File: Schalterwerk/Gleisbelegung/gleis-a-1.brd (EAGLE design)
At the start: 100 x 80 mm, 34 parts, among them J1 PHNX_4P_508CONN_1017493, J2 PHNX_4P_508CONN_1017493, J3 PHNX_2P_508CONN_1017491, J4 PHNX_4P_350CONN_1984989_PXC, J5 PHNX_4P_350CONN_1984989_PXC, Q1 P-MOSFET, Q2 P-MOSFET, Q3 P-MOSFET, Q4 P-MOSFET, X1 RJ45-JACK

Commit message: Updates the solder jumpers to connect neighboring traces on the bus side.
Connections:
- net N$26: now also SJ11.P$2
- net N$3: no longer SJ10.P$2, SJ11.P$2
- net N$6: now also SJ10.P$2
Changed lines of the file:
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@@
 <contactref element="J4" pad="1"/>
 <contactref element="SJ9" pad="P$2"/>
-<contactref element="SJ10" pad="P$2"/>
-<contactref element="SJ11" pad="P$2"/>
 <wire x1="-25.655" y1="-410.21" x2="-59.69" y2="-394.97" width="0" layer="19" extent="1-1"/>
 <wire x1="-114.554" y1="-421.64" x2="-59.69" y2="-394.97" width="0" layer="19" extent="1-1"/>
-<wire x1="-114.554" y1="-426.72" x2="-114.554" y2="-421.64" width="0" layer="19" extent="1-1"/>
-<wire x1="-114.554" y1="-431.8" x2="-114.554" y2="-426.72" width="0" layer="19" extent="1-1"/>
 <wire x1="3.81" y1="-10.16" x2="-59.69" y2="-394.97" width="0" layer="19" extent="1-1"/>
 </signal>
@@
 <contactref element="J4" pad="3"/>
 <contactref element="SJ9" pad="P$1"/>
+<contactref element="SJ10" pad="P$2"/>
 <wire x1="-27.695" y1="-410.21" x2="-52.69" y2="-394.97" width="0" layer="19" extent="1-1"/>
 <wire x1="-115.824" y1="-421.64" x2="-52.69" y2="-394.97" width="0" layer="19" extent="1-1"/>
+<wire x1="-114.554" y1="-426.72" x2="-115.824" y2="-421.64" width="0" layer="19" extent="1-1"/>
 <wire x1="8.89" y1="-10.16" x2="-52.69" y2="-394.97" width="0" layer="19" extent="1-1"/>
 </signal>
@@
 <contactref element="J5" pad="1"/>
 <contactref element="SJ10" pad="P$1"/>
+<contactref element="SJ11" pad="P$2"/>
 <wire x1="-115.824" y1="-426.72" x2="-99.06" y2="-394.97" width="0" layer="19" extent="1-1"/>
+<wire x1="-114.554" y1="-431.8" x2="-115.824" y2="-426.72" width="0" layer="19" extent="1-1"/>
 <wire x1="-28.715" y1="-408.43" x2="-99.06" y2="-394.97" width="0" layer="19" extent="1-1"/>
 <wire x1="13.97" y1="-10.16" x2="-28.715" y2="-408.43" width="0" layer="19" extent="1-1"/>

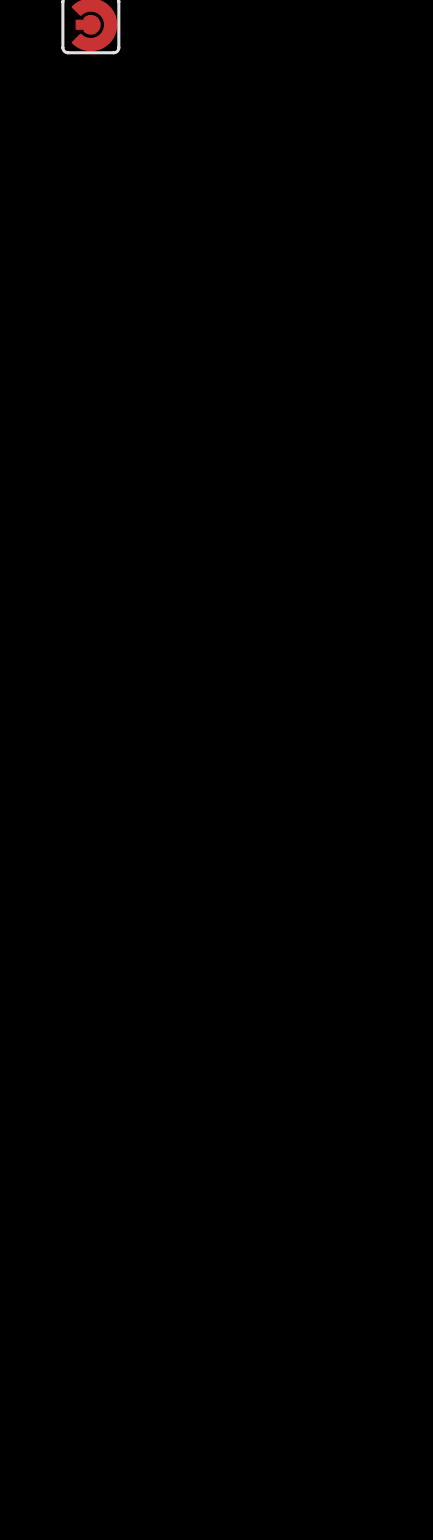
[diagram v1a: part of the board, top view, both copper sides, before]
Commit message: Updates the frames on the schematics with proper project information.
Adds LEDs for observing what is happening on the Gleisbelegtmeldung.
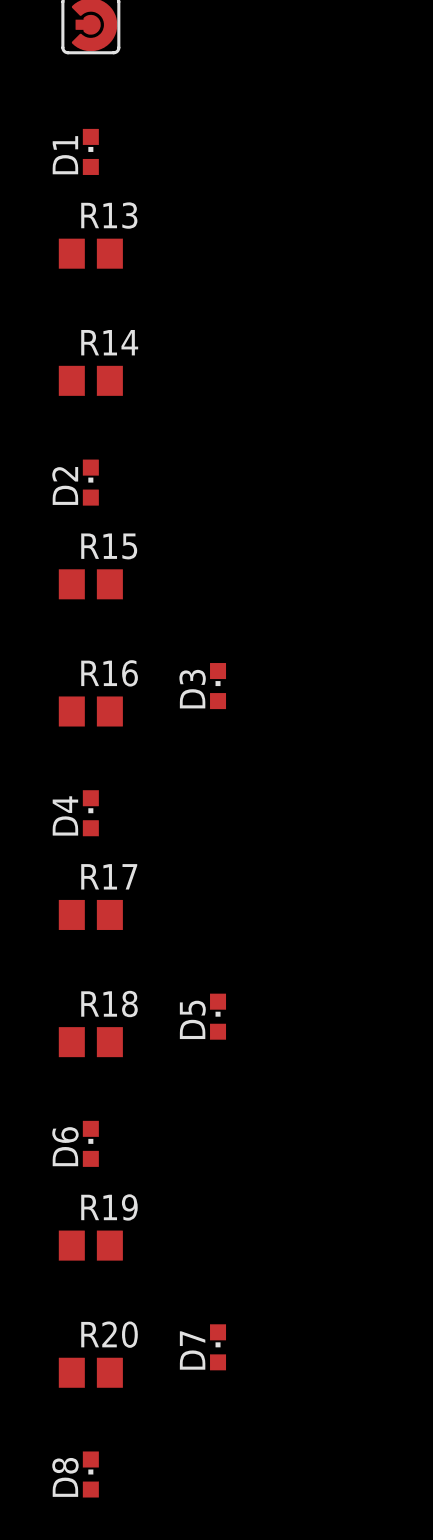
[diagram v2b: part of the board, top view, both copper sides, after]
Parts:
- added D1, D2, D3, D4, D5, D6, D7, D8: (no value), led:CHIPLED_0603
- added R13, R14, R15, R16, R17, R18, R19, R20: 1k5, rcl:R0805
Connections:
- new net N$21: D2.A, R14.1
- new net N$23: D3.A, R15.1
- new net N$24: D4.A, R16.1
- new net N$25: D5.A, R17.1
- new net N$27: D6.A, R18.1
- new net N$29: D7.A, R19.1
- new net N$30: D8.A, R20.1
- new net N$8: D1.A, R13.1
- net GND: now also D1.C, D2.C, D3.C, D4.C, D5.C, D6.C, D7.C, D8.C
- net N$1: now also R13.2, R14.2
- net N$10: now also R15.2, R16.2
- net N$11: now also R17.2, R18.2
- net N$13: now also R19.2, R20.2

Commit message: Adds component layout to the board. Routes the isolated part of the traces.
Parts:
- added H1, H2, H3, H4: MOUNT-HOLE3.3, holes:3,3
- added X2: IO-HAT, eagleparts:IOBOARD
- D2, D4, D6, D8: value (none) -> LEDHEADER; device led:CHIPLED_0603 -> eagleparts:LEDHEADER
- moved D8 522.2 mm to (12.7, 2.02), turned to 180 degrees
- moved D7 521.2 mm to (12.7, 8.89), turned to 90 degrees
- moved R19 519.1 mm to (17.8, 8.89)
- moved R20 519.1 mm to (17.8, 2.54)
- moved D6 508.9 mm to (22.9, 2.02), turned to 180 degrees
- moved D5 507.7 mm to (22.9, 8.89), turned to 90 degrees
- moved SJ11 507.1 mm to (81.3, 35.6), turned to 90 degrees
- moved SJ10 506.0 mm to (81.3, 39.4), turned to 90 degrees
- moved R18 505.9 mm to (27.9, 2.54)
- moved R17 505.9 mm to (27.9, 8.89)
- moved SJ9 504.8 mm to (81.3, 43.2), turned to 90 degrees
- moved D4 496.0 mm to (33.0, 2.02), turned to 180 degrees
- moved D3 494.6 mm to (33.0, 8.89), turned to 90 degrees
- moved R15 493.2 mm to (38.1, 8.89)
- moved R16 493.2 mm to (38.1, 2.54)
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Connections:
- new net 12V2: X2.P$22
- new net GND2: X2.P$21
- new net GND3: X2.P$11
- new net GND4: X2.P$12
- net +12V: now also X2.P$1
- net CH1-12VIN: now also J1.1, J1.2; no longer J1.7, J1.8
- net CH1-RELAY: now also J2.1, J2.2; no longer J2.7, J2.8
- net CH2-12VIN: now also J1.3, J1.4; no longer J1.5, J1.6
- net CH2-RELAY: now also J2.3, J2.4; no longer J2.5, J2.6
- net CH3-12VIN: now also J1.5, J1.6; no longer J1.3, J1.4
- net CH3-RELAY: now also J2.5, J2.6; no longer J2.3, J2.4
- net CH4-12VIN: now also J1.7, J1.8; no longer J1.1, J1.2
- net CH4-RELAY: now also J2.7, J2.8; no longer J2.1, J2.2
- net GND: now also X2.P$2
- net N$12: now also OK1.16, X2.P$17; no longer OK1.10
- net N$14: now also J5.3; no longer J5.2
- net N$15: now also J5.2, OK1.1; no longer J5.3, OK1.7
- net N$16: now also J5.1; no longer J5.4
- net N$17: now also OK1.8; no longer OK1.2
- net N$18: now also OK1.6; no longer OK1.4
- net N$19: now also OK1.2; no longer OK1.8
- net N$2: now also OK1.12, X2.P$19; no longer OK1.14
- net N$20: now also J4.1; no longer J4.4
- net N$26: now also J5.4, OK1.3; no longer J5.1, OK1.5
- net N$3: now also J4.4, OK1.7; no longer J4.1, OK1.1
- net N$4: now also J4.3; no longer J4.2
- net N$5: now also OK1.14, X2.P$18; no longer OK1.12
- net N$6: now also J4.2, OK1.5; no longer J4.3, OK1.3
- net N$7: now also OK1.4; no longer OK1.6
- net N$9: now also OK1.10, X2.P$20; no longer OK1.16
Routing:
- net N$3: track 0.00 -> 70.1 mm, vias 0 -> 3
- net +12V: track 0.00 -> 68.2 mm
- net CH4-12VIN: track 0.00 -> 63.2 mm
- net CH1-12VIN: track 0.00 -> 62.4 mm
- net N$15: track 0.00 -> 61.9 mm, vias 0 -> 1
- net CH3-12VIN: track 0.00 -> 61.3 mm
- net CH2-12VIN: track 0.00 -> 60.4 mm
- net N$6: track 0.00 -> 59.5 mm, vias 0 -> 3
- net N$16: track 0.00 -> 56.9 mm, vias 0 -> 1
- net N$4: track 0.00 -> 52.3 mm, vias 0 -> 1
- net GND: track 0.00 -> 52.2 mm
- net N$9: track 0.00 -> 51.5 mm
- net N$26: track 0.00 -> 51.3 mm, vias 0 -> 1
- net N$14: track 0.00 -> 44.2 mm, vias 0 -> 1
- net N$20: track 0.00 -> 42.3 mm, vias 0 -> 1
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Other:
- board size 100 x 80 mm -> 100.3 x 80 mm
- board text added: "+12V"
- board text added: "CH1 schalt"
- board text added: "CH1-12V"
- board text added: "CH1-OUT"
- board text added: "CH1-frei"
- board text added: "CH2 schalt"
- board text added: "CH2-12V"
- board text added: "CH2-OUT"
- board text added: "CH2-frei"
- board text added: "CH3 schalt"
- board text added: "CH3-12V"
- board text added: "CH3-OUT"
- board text added: "CH3-frei"
- board text added: "CH4 schalt"
- board text added: "CH4-12V"
- board text added: "CH4-OUT"
- board text added: "CH4-frei"
- board text added: "GND"
- board text added: "V+"

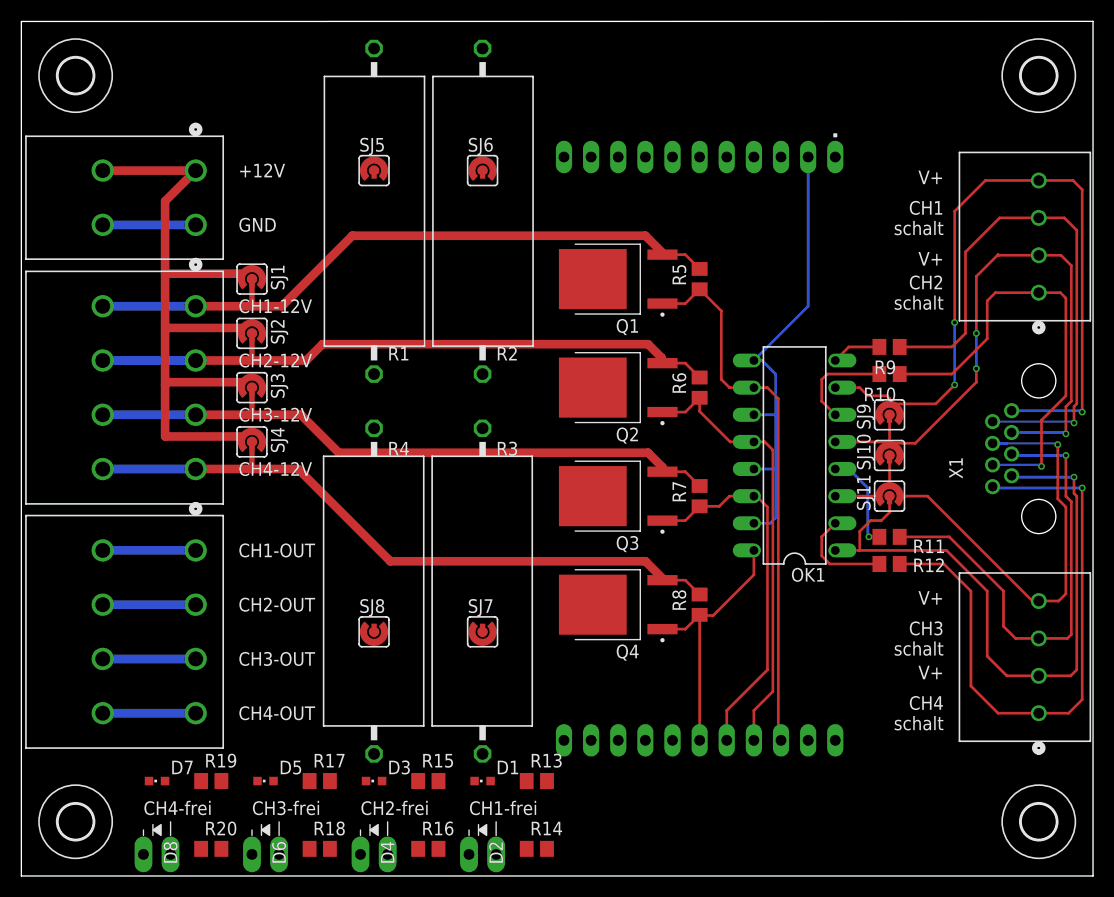
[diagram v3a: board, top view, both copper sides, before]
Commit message: Finishes routing and adds ground pour.
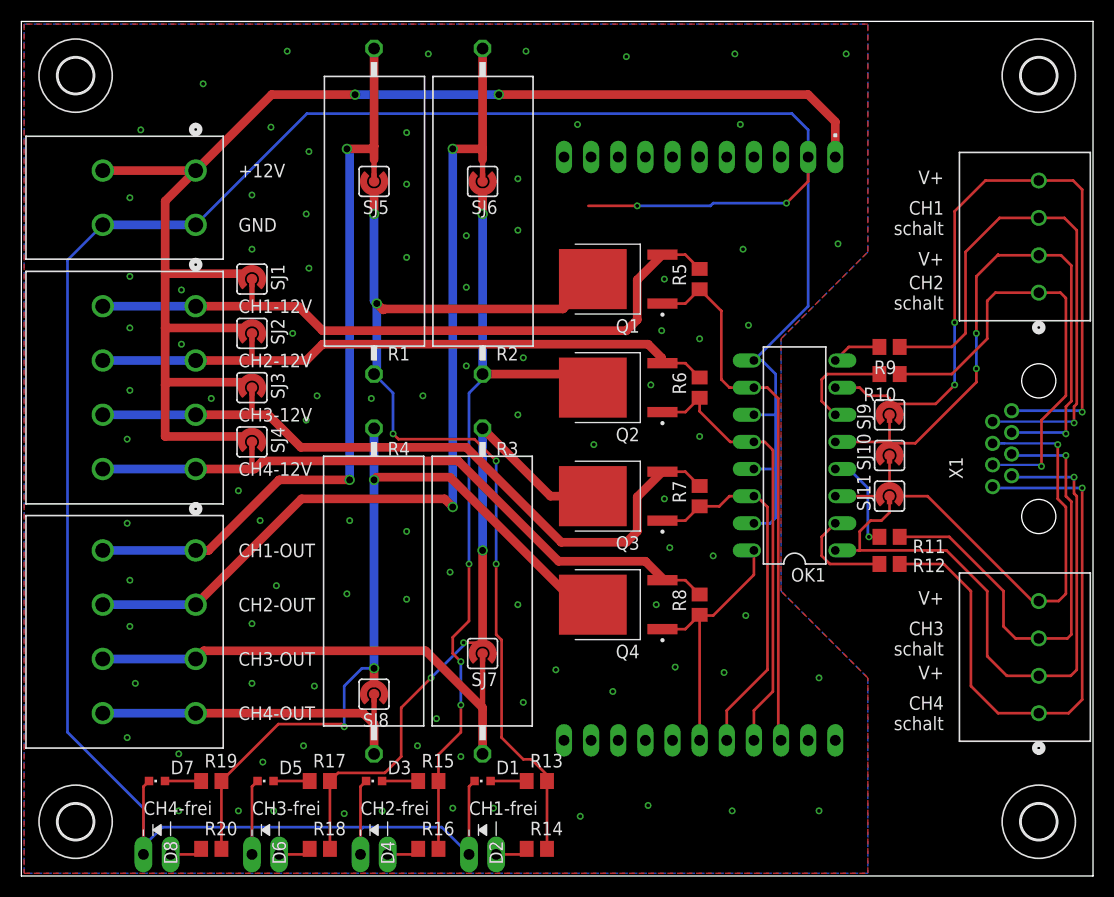
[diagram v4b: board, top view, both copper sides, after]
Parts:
- moved SJ8 5.84 mm to (33.0, 17.0), turned to 90 degrees
- moved SJ7 2.03 mm to (43.2, 20.8), turned to 90 degrees
- moved SJ5 1.02 mm to (33.0, 65.0), turned to 270 degrees
- moved SJ6 1.02 mm to (43.2, 65.0), turned to 270 degrees
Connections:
- removed net GND2: X2.P$21
- removed net GND3: X2.P$11
- removed net GND4: X2.P$12
- net GND: now also X2.P$11, X2.P$12, X2.P$21
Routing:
- net GND: track 52.2 -> 270.7 mm, vias 0 -> 95
- net N$1: track 0.00 -> 94.6 mm, vias 0 -> 5
- net CH2-RELAY: track 8.70 -> 85.7 mm, vias 0 -> 2
- net N$13: track 0.00 -> 76.9 mm, vias 0 -> 3
- net N$10: track 0.00 -> 74.7 mm, vias 0 -> 4
- net +12V: track 68.2 -> 135.4 mm, vias 0 -> 2
- net CH1-RELAY: track 8.70 -> 71.8 mm, vias 0 -> 2
- net N$11: track 0.00 -> 61.8 mm, vias 0 -> 3
- net CH3-RELAY: track 8.70 -> 47.2 mm
- net CH4-RELAY: track 8.70 -> 31.2 mm
- net CH3-12VIN: track 61.3 -> 68.3 mm
- net N$8: track 0.00 -> 3.38 mm
- net N$29: track 0.00 -> 3.38 mm
- net N$25: track 0.00 -> 3.38 mm
- net N$23: track 0.00 -> 3.38 mm
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- added copper zone on layer 1, net GND
- added copper zone on layer 16, net GND

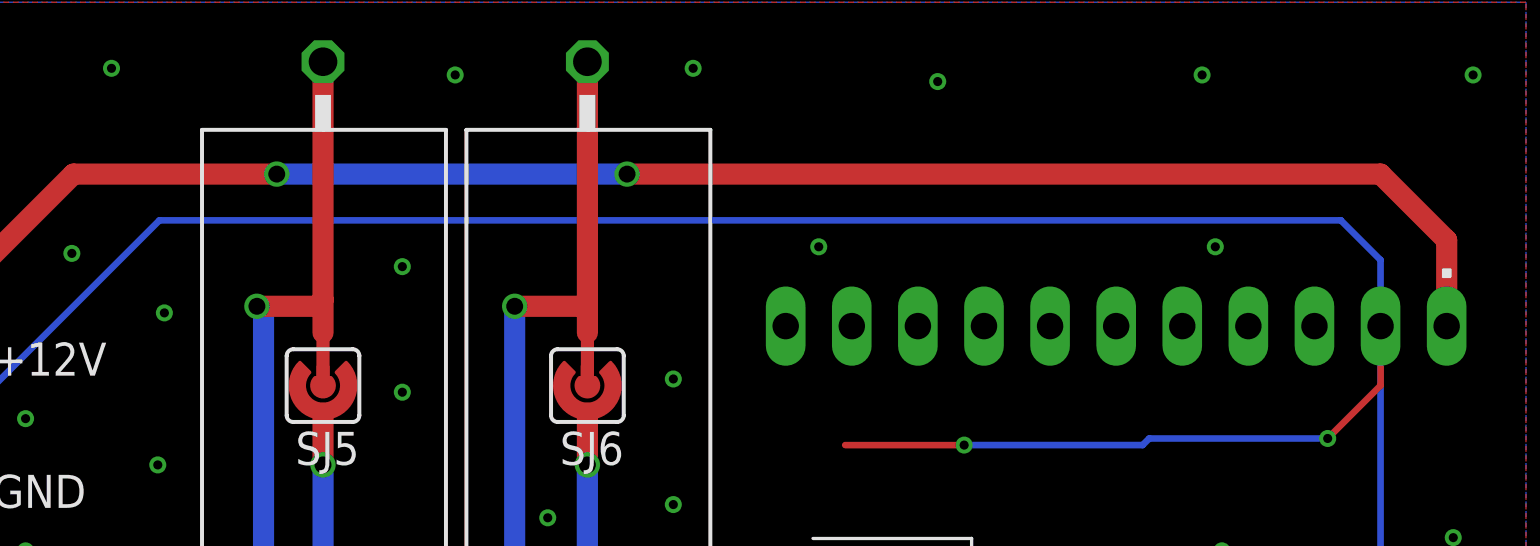
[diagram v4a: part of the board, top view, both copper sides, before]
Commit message: Updates the footprint of the daughterboard.
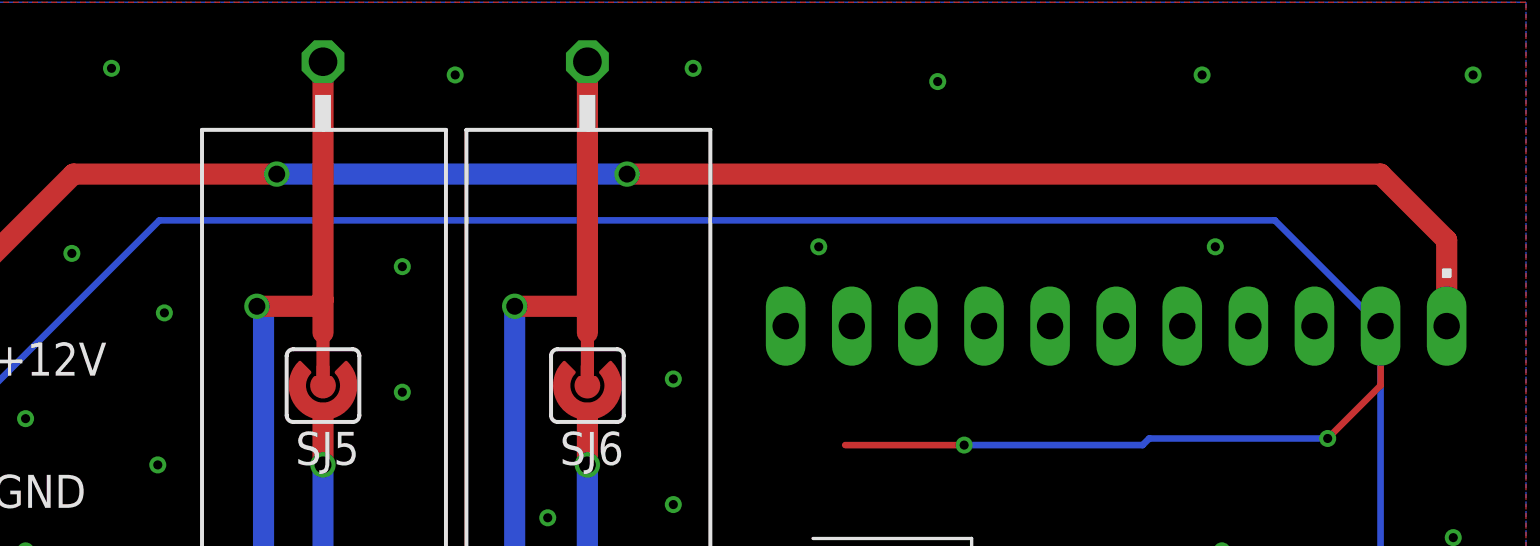
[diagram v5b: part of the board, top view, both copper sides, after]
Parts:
- moved X2 2.54 mm to (48.3, 80.0)
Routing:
- net GND: track 270.7 -> 269.2 mm
